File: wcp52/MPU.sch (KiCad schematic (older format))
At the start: 57 parts, among them J6 JLINK, J8 AVR-ICSP, U12 ATSAM4S16CA-AU, U18 ATMEGA32U4-AU-DNP, X2 12MHz

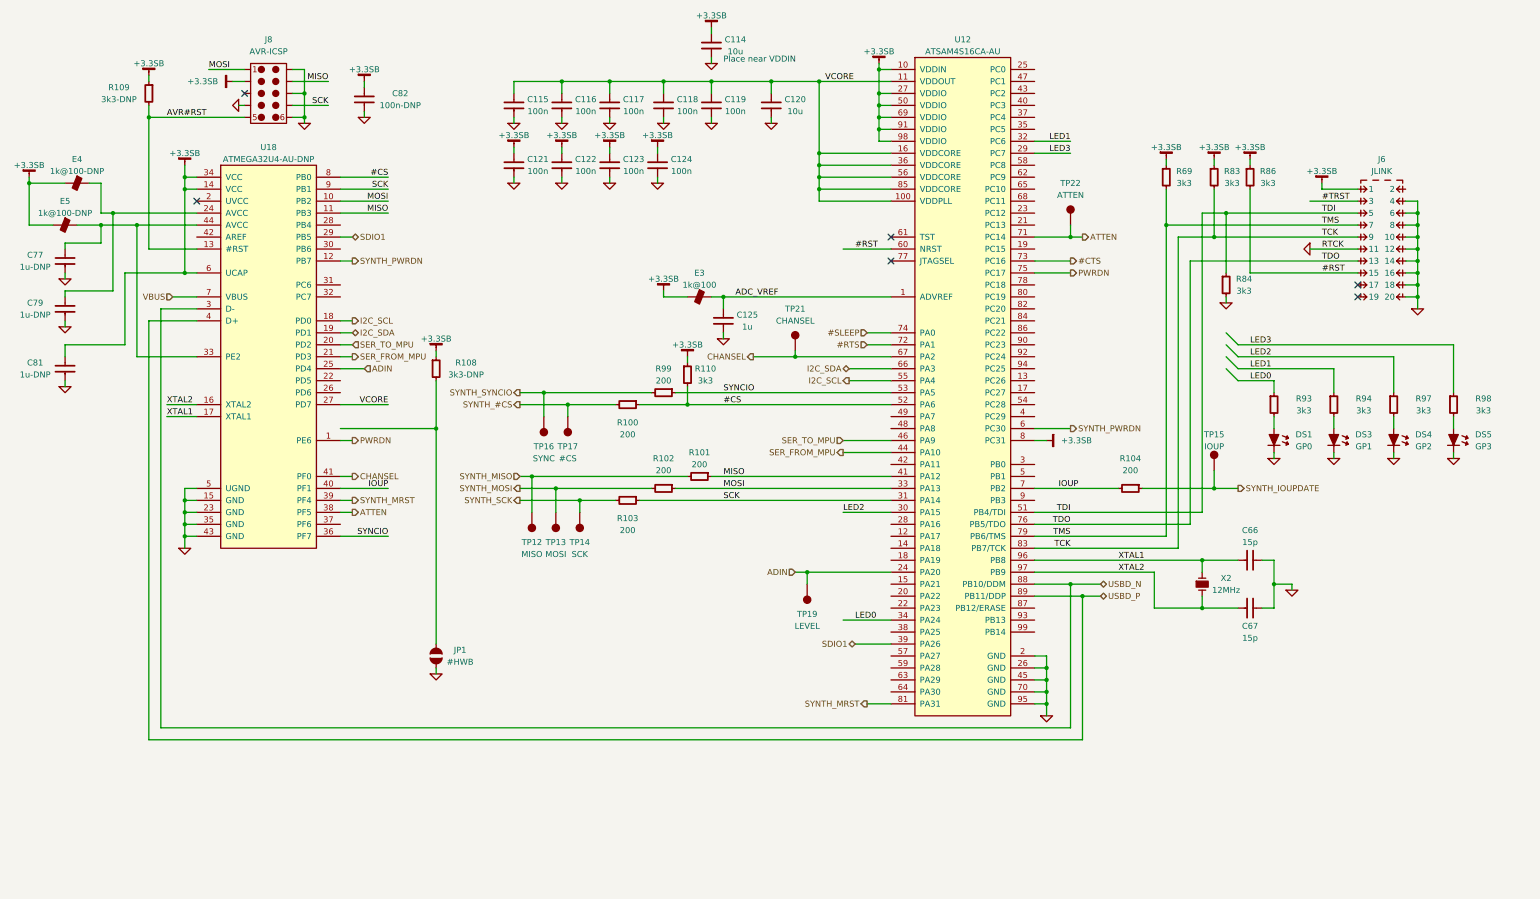
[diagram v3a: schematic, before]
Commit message: Reorganize MPU schematic
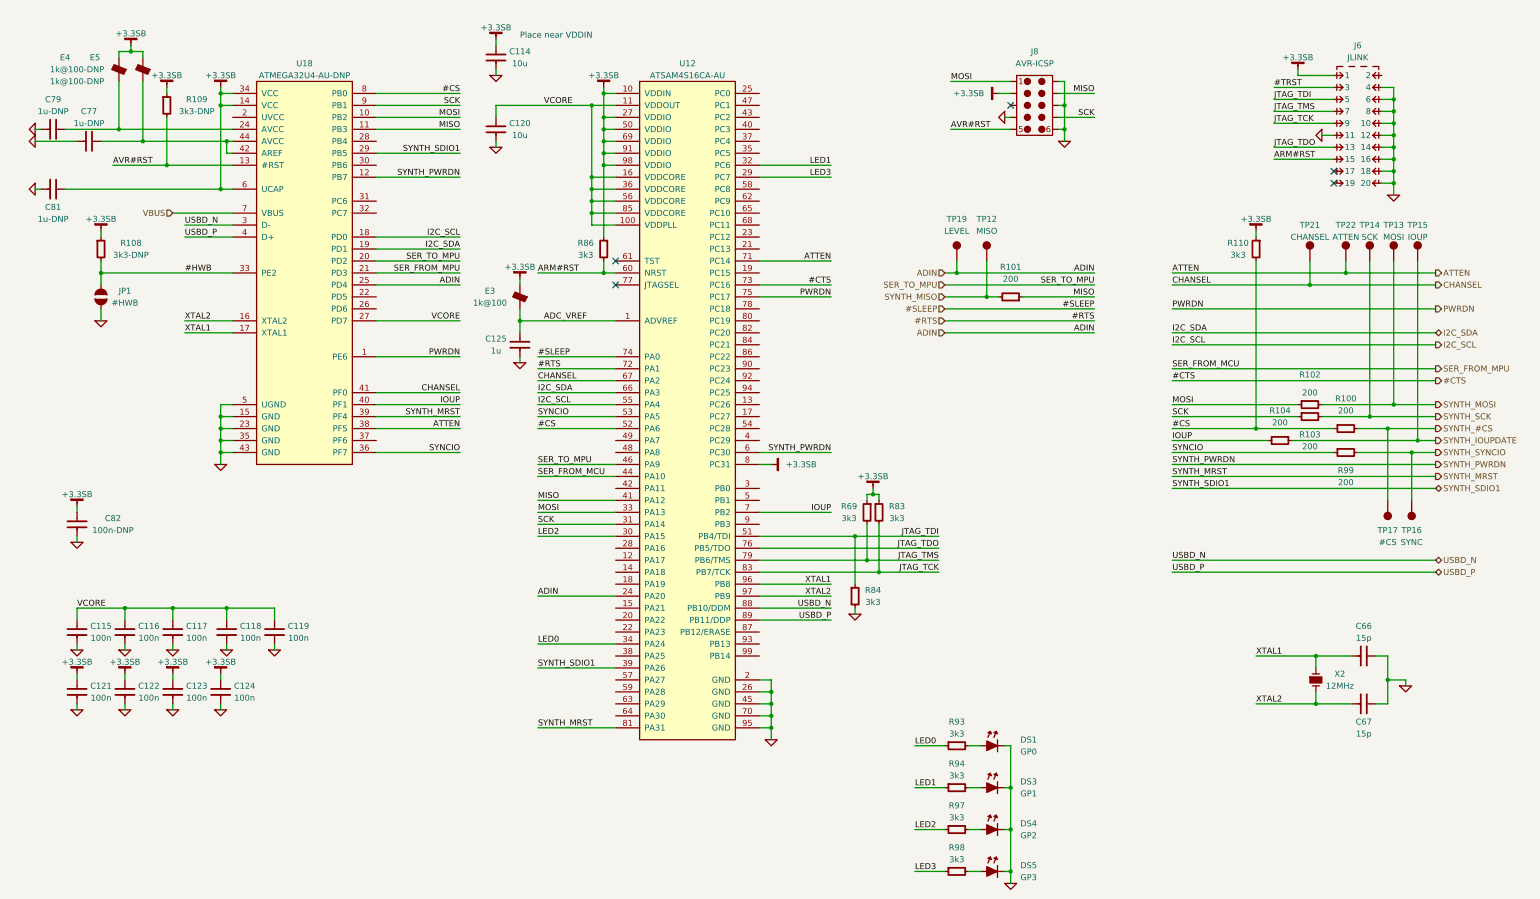
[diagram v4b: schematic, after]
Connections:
- net at C77.1, E5.2, U18.44 (AVCC): now also U18.42 (AREF); no longer U18.33 (PE2)
- net #HWB: now reaches JP1.1, R108.2
- net #HWB: now also U18.33 (PE2)
- net #RST renamed ARM#RST
- net SDIO1 renamed SYNTH_SDIO1
- net TCK renamed JTAG_TCK
- net TDI renamed JTAG_TDI
- net TDO renamed JTAG_TDO
- net TMS renamed JTAG_TMS
- no-connect marks 6 -> 5
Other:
- moved on the sheet: C114, C115, C116, C117, C118, C119, C120, C121, C122, C123, C124, C125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

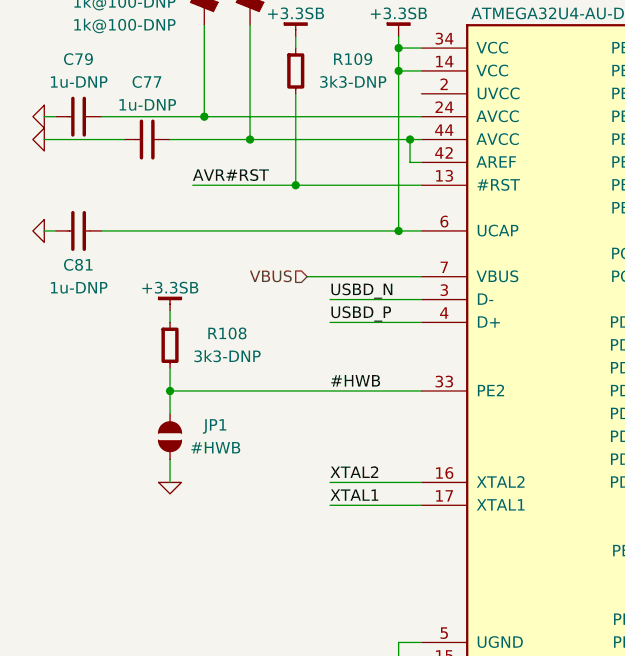
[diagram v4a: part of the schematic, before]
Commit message: Add reset jumper
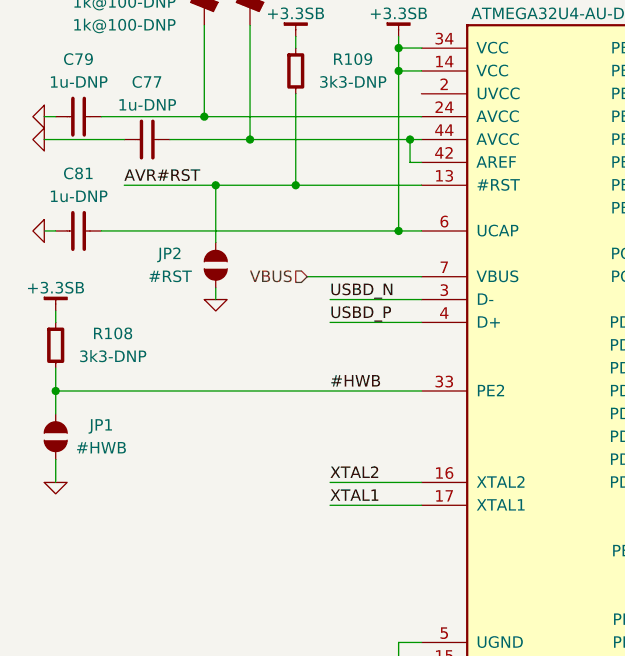
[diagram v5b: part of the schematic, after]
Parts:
- added JP2: #RST, symbol JUMPER-SOLDER
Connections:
- net AVR#RST: now also JP2.1
- net GND: now also JP2.2
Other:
- moved on the sheet: JP1, R108
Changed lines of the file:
@@
 U 1 1 5500CAF6
 P 900 2100
-F 0 "C81" V 750 2100 50  0000 C CNN
-F 1 "1u-DNP" V 650 2100 50  0000 C CNN
+F 0 "C81" V 1150 2100 50  0000 C CNN
+F 1 "1u-DNP" V 1050 2100 50  0000 C CNN
 F 2 "IPC7351-Nominal:CAPC2012X70" H 900 2100 50  0001 C CNN
 F 3 "" H 890 2075 60  0000 C CNN
@@
 L JUMPER-SOLDER JP1
 U 1 1 5503624F
-P 1300 3000
-F 0 "JP1" V 1250 3200 50  0000 C CNN
-F 1 "#HWB" V 1350 3200 50  0000 C CNN
-F 2 "" H 1300 3000 60  0000 C CNN
-F 3 "" H 1300 3000 60  0000 C CNN
-	1    1300 3000
+P 800 3000
+F 0 "JP1" V 750 3200 50  0000 C CNN
+F 1 "#HWB" V 850 3200 50  0000 C CNN
+F 2 "" H 800 3000 60  0000 C CNN
+F 3 "" H 800 3000 60  0000 C CNN
+	1    800  3000
 	0    1    1    0
 $EndComp
@@
 L R-0603 R108
 U 1 1 55036BC9
-P 1300 2600
-F 0 "R108" H 1550 2650 50  0000 C CNN
-F 1 "3k3-DNP" H 1550 2550 50  0000 C CNN
-F 2 "IPC7351-Nominal:RESC1608X50" H 1300 2600 50  0001 C CNN
-F 3 "" H 1300 2650 60  0000 C CNN
-F 4 "Value" H 1300 2600 60  0001 C CNN "Manuf"
-F 5 "#RES SMD 3.3k 5% [0603]" H 2050 3150 60  0001 C CNN "BOM"
-	1    1300 2600
+P 800 2600
+F 0 "R108" H 1050 2650 50  0000 C CNN
+F 1 "3k3-DNP" H 1050 2550 50  0000 C CNN
+F 2 "IPC7351-Nominal:RESC1608X50" H 800 2600 50  0001 C CNN
+F 3 "" H 800 2650 60  0000 C CNN
+F 4 "Value" H 800 2600 60  0001 C CNN "Manuf"
+F 5 "#RES SMD 3.3k 5% [0603]" H 1550 3150 60  0001 C CNN "BOM"
+	1    800  2600
 	1    0    0    -1
 $EndComp
@@
 	1    0    0    -1
 $EndComp
-Text Label 1400 1900 0    50   ~ 0
+Text Label 1100 1900 0    50   ~ 0
 AVR#RST
 Text HLabel 1900 2300 0    50   Input ~ 0
@@
 L +3.3SB #PWR0248
 U 1 1 55032B85
-P 1300 2450
-F 0 "#PWR0248" H 1300 2500 30  0001 C CNN
-F 1 "+3.3SB" H 1300 2550 50  0000 C CNN
-F 2 "" H 1300 2450 60  0000 C CNN
-F 3 "" H 1300 2450 60  0000 C CNN
-	1    1300 2450
+P 800 2450
+F 0 "#PWR0248" H 800 2500 30  0001 C CNN
+F 1 "+3.3SB" H 800 2550 50  0000 C CNN
+F 2 "" H 800 2450 60  0000 C CNN
+F 3 "" H 800 2450 60  0000 C CNN
+	1    800  2450
 	1    0    0    -1
 $EndComp
@@
 L GND #PWR0249
 U 1 1 5503374C
-P 1300 3200
-F 0 "#PWR0249" H 1300 3200 30  0001 C CNN
-F 1 "GND" H 1300 3130 30  0001 C CNN
-F 2 "" H 1300 3200 60  0000 C CNN
-F 3 "" H 1300 3200 60  0000 C CNN
-	1    1300 3200
+P 800 3200
+F 0 "#PWR0249" H 800 3200 30  0001 C CNN
+F 1 "GND" H 800 3130 30  0001 C CNN
+F 2 "" H 800 3200 60  0000 C CNN
+F 3 "" H 800 3200 60  0000 C CNN
+	1    800  3200
 	1    0    0    -1
 $EndComp
@@
 	1850 1500 1850 1900
 Wire Wire Line
-	1400 1900 2400 1900
+	1100 1900 2400 1900
 Wire Wire Line
 	1850 1250 1850 1300
@@
 	4300 3500 3600 3500
 Wire Wire Line
-	2400 2800 1300 2800
-Wire Wire Line
-	1300 2700 1300 2900
-Wire Wire Line
-	1300 2450 1300 2500
-Connection ~ 1300 2800
-Wire Wire Line
-	1300 3200 1300 3100
+	2400 2800 800  2800
+Wire Wire Line
+	800  2700 800  2900
+Wire Wire Line
+	800  2450 800  2500
+Connection ~ 800  2800
+Wire Wire Line
+	800  3200 800  3100
 Wire Wire Line
 	4300 3200 3600 3200
@@
 VCORE
 Connection ~ 11400 2900
+$Comp
+L JUMPER-SOLDER JP2
+U 1 1 550B520B
+P 1500 2250
+F 0 "JP2" V 1450 2450 50  0000 C CNN
+F 1 "#RST" V 1550 2450 50  0000 C CNN
+F 2 "" H 1500 2250 60  0000 C CNN
+F 3 "" H 1500 2250 60  0000 C CNN
+	1    1500 2250
+	0    -1   1    0
+$EndComp
+Wire Wire Line
+	1500 2150 1500 1900
+Connection ~ 1500 1900
+$Comp
+L GND #PWR0261
+U 1 1 550B5671
+P 1500 2400
+F 0 "#PWR0261" H 1500 2400 30  0001 C CNN
+F 1 "GND" H 1500 2330 30  0001 C CNN
+F 2 "" H 1500 2400 60  0000 C CNN
+F 3 "" H 1500 2400 60  0000 C CNN
+	1    1500 2400
+	1    0    0    -1
+$EndComp
+Wire Wire Line
+	1500 2400 1500 2350
 $EndSCHEMATC

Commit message: Connect #SLEEP to AVR
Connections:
- net #SLEEP: now also U18.32 (PC7)
- no-connect marks 5 -> 6
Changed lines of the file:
@@
 Wire Wire Line
 	1500 2400 1500 2350
+NoConn ~ 2400 1500
+Text Label 4300 2300 2    50   ~ 0
+#SLEEP
+Wire Wire Line
+	4300 2300 3600 2300
 $EndSCHEMATC

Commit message: Route LEDs to AVR
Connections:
- net LED0: now also U12.42 (PA11), U18.30 (PB6)
- net LED1: now also U12.43 (PC2), U18.31 (PC6)
- net LED2: now also U12.23 (PC12), U18.26 (PD6)
- net LED3: now also U12.21 (PC13), U18.22 (PD5)
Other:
- note added: "@U18 is an alternative microcontroller. Not used in first revision.\nNote duplicate connections. These are used to facilitate routing. Make\nsure to set all duplicate connections as inputs."

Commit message: Remove extra connections
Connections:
- net LED0: no longer U12.34 (PA24)
- net LED1: no longer U12.32 (PC6)
- net LED2: no longer U12.30 (PA15)
- net LED3: no longer U12.29 (PC7)
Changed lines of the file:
@@
 Text Label 4950 4900 0    50   ~ 0
 SCK
-Text Label 4950 5000 0    50   ~ 0
-LED2
 Text Label 4950 5500 0    50   ~ 0
 ADIN
-Text Label 4950 5900 0    50   ~ 0
-LED0
 Text Label 4950 6100 0    50   ~ 0
 SYNTH_SDIO1
@@
 Text Label 7400 2700 2    50   ~ 0
 ATTEN
-Text Label 7400 2000 2    50   ~ 0
-LED3
-Text Label 7400 1900 2    50   ~ 0
-LED1
 Text Label 8400 1200 0    50   ~ 0
 MOSI
@@
 Connection ~ 1550 950
 Wire Wire Line
-	1850 1500 1850 1900
+	1850 1900 1850 1500
 Wire Wire Line
 	1100 1900 2400 1900
@@
 	4950 4900 5600 4900
 Wire Wire Line
-	4950 5000 5600 5000
-Wire Wire Line
 	4950 5500 5600 5500
-Wire Wire Line
-	4950 5900 5600 5900
 Wire Wire Line
 	4950 6100 5600 6100
@@
 	7400 2700 6800 2700
 Wire Wire Line
-	7400 2000 6800 2000
-Wire Wire Line
-	7400 1900 6800 1900
-Wire Wire Line
 	8400 1200 8900 1200
